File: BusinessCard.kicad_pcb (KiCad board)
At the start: 2 copper layers, 51 x 89 mm, 203 parts, among them J1 Conn_01x03_Socket, J2 Conn_01x04_Socket, J3 Conn_01x02, SW1 Up, SW2 Left, SW3 Down, SW4 Right, SW5 A, SW6 B, U1 STM32F103C8T6

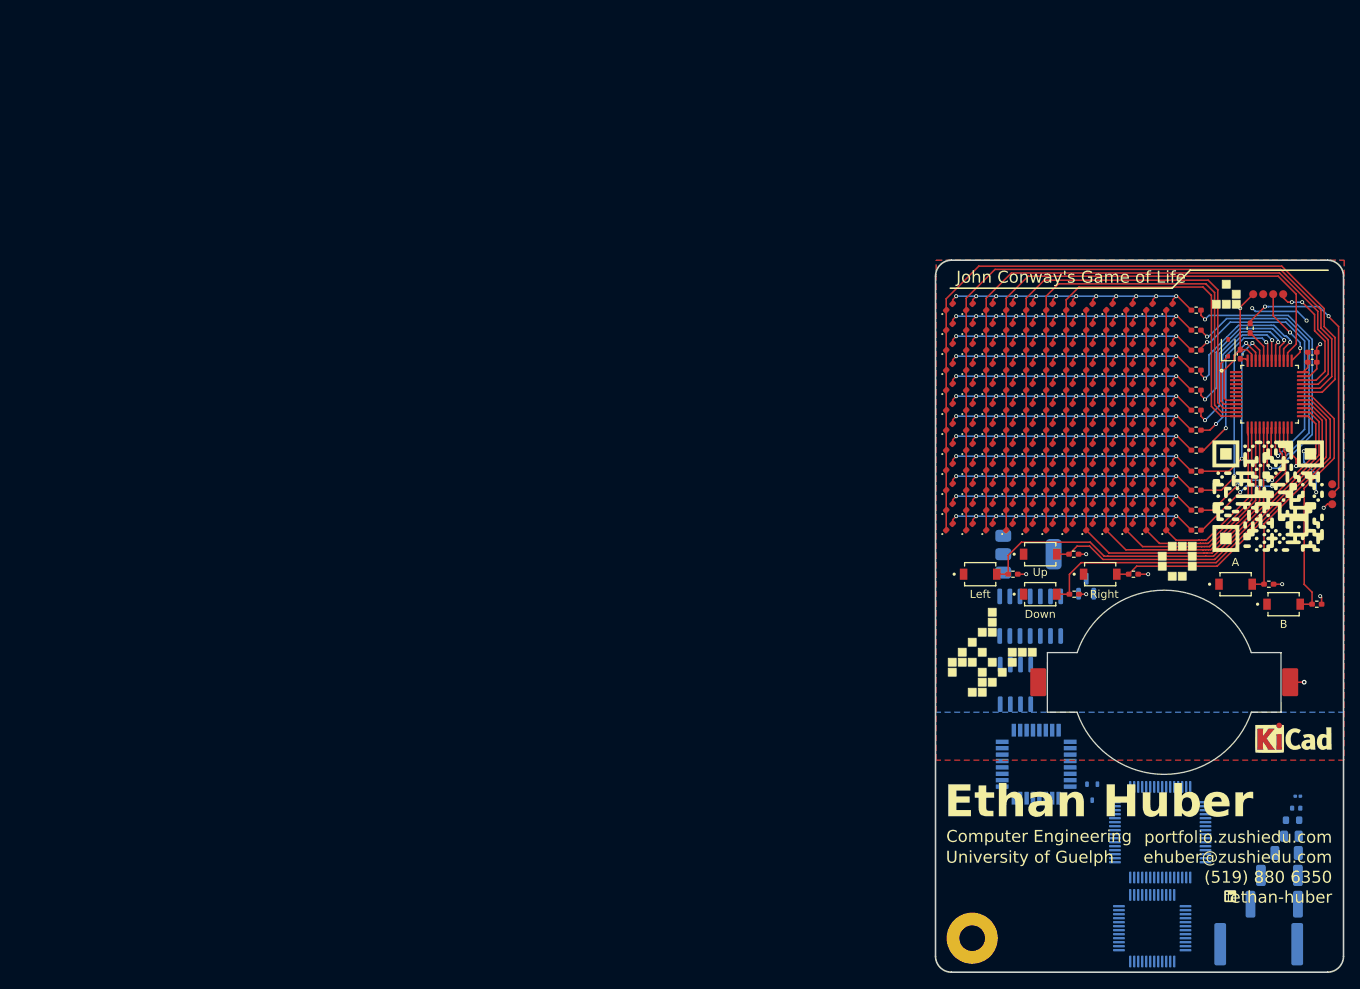
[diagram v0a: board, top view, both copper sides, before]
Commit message: Switched LED footprint and fixed row traces
- Switched LED footprints from 0402 to 0603 to reduce assembly cost
- Added back row traces that were accidentally removed in an earlier commit
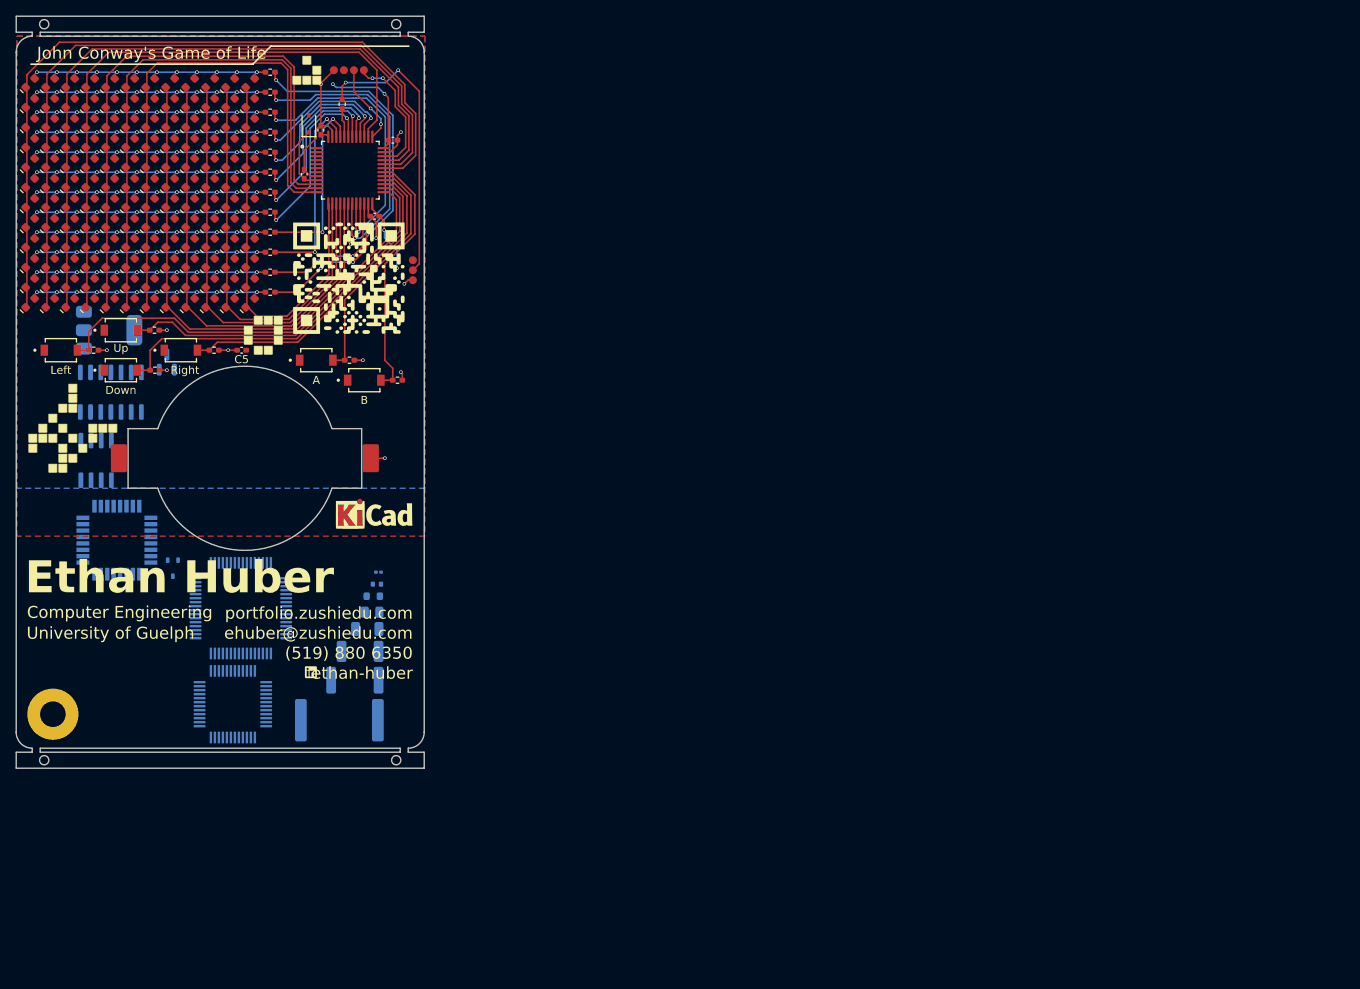
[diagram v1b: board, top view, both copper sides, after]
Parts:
- removed the G*** at (179.6, 107.7) (x3)
- removed the G*** at (176.5, 77.5)
- removed the G*** at (171.8, 127.5)
- removed the G*** at (158.0, 66.5)
- removed the G*** at (182.0, 101.5)
- removed the G*** at (182.0, 94.5)
- removed the G*** at (179.5, 108.0)
- added C4: 100 nF, Capacitor_SMD:C_0402_1005Metric_Pad0.74x0.62mm_HandSolder, F.Cu at (56.0, 37.2)
- added C5: 4.7 uF, Capacitor_SMD:C_0402_1005Metric_Pad0.74x0.62mm_HandSolder, F.Cu at (48.2, 59.2)
- added G*** (x3): LOGO, LOGO, F.Cu at (64.7, 79.7)
- added G***: LOGO, LOGO, F.Cu at (56.8, 99.5)
- added G***: LOGO, LOGO, F.Cu at (61.6, 50.2)
- added G***: LOGO, LOGO, B.Cu at (43.0, 38.5)
- added G***: LOGO, LOGO, B.Cu at (67.1, 73.5)
- added G***: LOGO, LOGO, B.Cu at (64.6, 80.0)
- added G***: LOGO, LOGO, B.Cu at (67.1, 66.5)
- added REF**: MountingHole, Dependencies:MountingHole, F.Cu at (23.5, 110.5)
- added REF**: MountingHole, Dependencies:MountingHole, F.Cu at (23.5, 18.5)
- added REF**: MountingHole, Dependencies:MountingHole, F.Cu at (67.5, 110.5)
- added REF**: MountingHole, Dependencies:MountingHole, F.Cu at (67.5, 18.5)
- C3: value 4.7 uF -> 100 nF
- D10, D100, D101, D102, D103, D104, D105, D106, D107, D108, D109, D11, D110, D111, D112, D113, D114, D115, D116, D117, D118, D119, D12, D120, D121, D122, D123, D124, D125, D126, D127, D128, D129, D13, D130, D131, D132, D133, D134, D135, D136, D137, D138, D139, D14, D140, D141, D142, D143, D144, D145, D15, D16, D17, D18, D19, D2, D20, D21, D22, D23, D24, D25, D26, D27, D28, D29, D3, D30, D31, D32, D33, D34, D35, D36, D37, D38, D39, D4, D40, D41, D42, D43, D44, D45, D46, D47, D48, D49, D5, D50, D51, D52, D53, D54, D55, D56, D57, D58, D59, D6, D60, D61, D62, D63, D64, D65, D66, D67, D68, D69, D7, D70, D71, D72, D73, D74, D75, D76, D77, D78, D79, D8, D80, D81, D82, D83, D84, D85, D86, D87, D88, D89, D9, D90, D91, D92, D93, D94, D95, D96, D97, D98, D99: footprint Dependencies:LED_0402_1005Metric_Pad0.77x0.64mm_HandSolder_Notext -> Dependencies:LED_0603_1608Metric_Notext
- moved R16 119.5 mm to (51.8, 44.5)
- moved R10 119.5 mm to (51.8, 29.5)
- moved R11 119.5 mm to (51.8, 32.0)
- moved R12 119.5 mm to (51.8, 34.5)
- moved R13 119.5 mm to (51.8, 37.0)
- moved R14 119.5 mm to (51.8, 39.5)
- moved R15 119.5 mm to (51.8, 42.0)
- moved R17 119.5 mm to (51.8, 47.0)
- moved R18 119.5 mm to (51.8, 49.5)
- moved R19 119.5 mm to (51.8, 52.0)
- moved R8 119.5 mm to (51.8, 24.5)
- moved R9 119.5 mm to (51.8, 27.0)
- moved C3 118.4 mm to (64.8, 42.5), turned to 180 degrees
- moved REF** 118.3 mm to (63.0, 96.9)
- moved REF** 118.3 mm to (63.9, 94.1)
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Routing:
- net +3.3V: track 17.0 -> 24.6 mm
- net R6: track 22.2 -> 20.3 mm
- net Net-(D100-A): track 43.6 -> 42.0 mm
- net Net-(D26-A): track 43.5 -> 42.0 mm
- net Net-(D14-A): track 43.5 -> 42.0 mm
- net Net-(D10-A): track 43.5 -> 42.0 mm
- net Net-(D50-A): track 43.5 -> 42.0 mm
- net Net-(D38-A): track 43.5 -> 42.0 mm
- net Net-(D74-A): track 43.5 -> 42.0 mm
- net Net-(D62-A): track 43.5 -> 42.0 mm
- net Net-(D134-A): track 43.5 -> 42.0 mm
- net Net-(D122-A): track 43.5 -> 42.0 mm
- net Net-(D110-A): track 43.5 -> 42.0 mm
- net Net-(D86-A): track 43.5 -> 42.0 mm
- net Net-(J1-Pin_2): track 34.4 -> 35.9 mm
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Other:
- board size 51 x 89 mm -> 51 x 94 mm
